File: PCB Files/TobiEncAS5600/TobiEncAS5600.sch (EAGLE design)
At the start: 4 parts

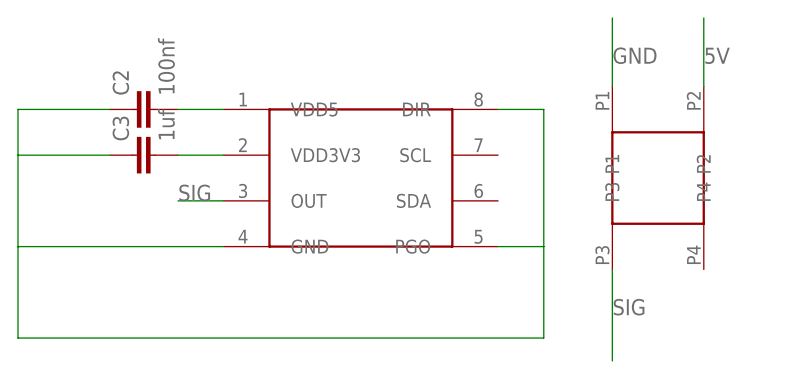
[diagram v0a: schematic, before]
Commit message: position components for wider encoder board
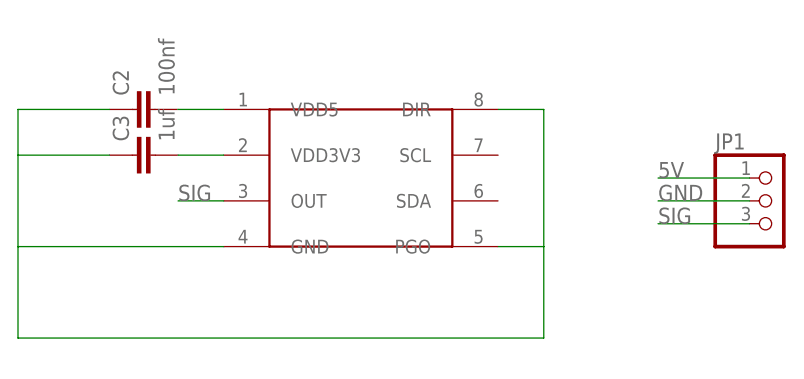
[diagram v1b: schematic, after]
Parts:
- removed U$2: DF11-4PIN, Gavin:DF11-4PIN
- added JP1: (no value), pinhead:PINHD-1X3
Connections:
- net N$1 renamed VDD3V3
- net 5V: now also JP1.1; no longer U$2.P2
- net GND: now also JP1.2; no longer U$2.P1
- net SIG: now also JP1.3; no longer U$2.P3
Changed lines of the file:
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@@
 <?xml version="1.0" encoding="utf-8"?>
 <!DOCTYPE eagle SYSTEM "eagle.dtd">
-<eagle version="6.4">
+<eagle version="8.5.2">
 <drawing>
 <settings>
-<setting alwaysvectorfont="yes"/>
+<setting alwaysvectorfont="no"/>
+<setting keepoldvectorfont="yes"/>
 <setting verticaltext="up"/>
 </settings>
@@
 </classes>
 <parts>
-<part name="U$2" library="Gavin" deviceset="DF11-4PIN" device=""/>
 <part name="U$1" library="Gavin" deviceset="AS5600" device=""/>
 <part name="C2" library="SparkFun-Capacitors" deviceset="CAP" device="0603-CAP" value="100nf"/>
 <part name="C3" library="SparkFun-Capacitors" deviceset="CAP" device="0603-CAP" value="1uf"/>
+<part name="JP1" library="pinhead" library_urn="urn:adsk.eagle:library:325" deviceset="PINHD-1X3" device=""/>
 </parts>
 <sheets>
@@
 </plain>
 <instances>
-<instance part="U$2" gate="G$1" x="106.68" y="60.96"/>
 <instance part="U$1" gate="G$1" x="73.66" y="60.96"/>
 <instance part="C2" gate="G$1" x="50.8" y="68.58" rot="R90"/>
 <instance part="C3" gate="G$1" x="50.8" y="63.5" rot="R90"/>
+<instance part="JP1" gate="A" x="119.38" y="58.42"/>
 </instances>
 <busses>
@@
 <net name="5V" class="0">
 <segment>
-<pinref part="U$2" gate="G$1" pin="P2"/>
-<wire x1="111.76" y1="71.12" x2="111.76" y2="78.74" width="0.1524" layer="91"/>
-<label x="111.76" y="73.66" size="1.778" layer="95"/>
-</segment>
-<segment>
 <pinref part="U$1" gate="G$1" pin="VDD5"/>
 <wire x1="58.42" y1="68.58" x2="53.34" y2="68.58" width="0.1524" layer="91"/>
 <pinref part="C2" gate="G$1" pin="2"/>
 </segment>
+<segment>
+<pinref part="JP1" gate="A" pin="1"/>
+<wire x1="116.84" y1="60.96" x2="106.68" y2="60.96" width="0.1524" layer="91"/>
+<label x="106.68" y="60.96" size="1.778" layer="95"/>
+</segment>
 </net>
 <net name="SIG" class="0">
-<segment>
-<pinref part="U$2" gate="G$1" pin="P3"/>
-<wire x1="101.6" y1="40.64" x2="101.6" y2="50.8" width="0.1524" layer="91"/>
-<label x="101.6" y="45.72" size="1.778" layer="95"/>
-</segment>
 <segment>
 <pinref part="U$1" gate="G$1" pin="OUT"/>
@@
 <label x="53.34" y="58.42" size="1.778" layer="95"/>
 </segment>
+<segment>
+<pinref part="JP1" gate="A" pin="3"/>
+<wire x1="116.84" y1="55.88" x2="106.68" y2="55.88" width="0.1524" layer="91"/>
+<label x="106.68" y="55.88" size="1.778" layer="95"/>
+</segment>
 </net>
 <net name="GND" class="0">
-<segment>
-<pinref part="U$2" gate="G$1" pin="P1"/>
-<wire x1="101.6" y1="78.74" x2="101.6" y2="71.12" width="0.1524" layer="91"/>
-<label x="101.6" y="73.66" size="1.778" layer="95"/>
-</segment>
 <segment>
 <pinref part="C2" gate="G$1" pin="1"/>
@@
 <wire x1="45.72" y1="63.5" x2="35.56" y2="63.5" width="0.1524" layer="91"/>
 </segment>
-</net>
-<net name="N$1" class="0">
+<segment>
+<pinref part="JP1" gate="A" pin="2"/>
+<wire x1="116.84" y1="58.42" x2="106.68" y2="58.42" width="0.1524" layer="91"/>
+<label x="106.68" y="58.42" size="1.778" layer="95"/>
+</segment>
+</net>
+<net name="VDD3V3" class="0">
 <segment>
 <pinref part="C3" gate="G$1" pin="2"/>
@@
 </schematic>
 </drawing>
+<compatibility>
+<note version="8.2" severity="warning">
+Since Version 8.2, EAGLE supports online libraries. The ids
+of those online libraries will not be understood (or retained)
+with this version.
+</note>
+</compatibility>
 </eagle>

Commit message: double wide encoder board
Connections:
- net GND: now also U$1.SCL, U$1.SDA
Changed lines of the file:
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@@
 <pinref part="U$1" gate="G$1" pin="DIR"/>
 <wire x1="88.9" y1="68.58" x2="93.98" y2="68.58" width="0.1524" layer="91"/>
-<wire x1="93.98" y1="68.58" x2="93.98" y2="53.34" width="0.1524" layer="91"/>
+<wire x1="93.98" y1="68.58" x2="93.98" y2="63.5" width="0.1524" layer="91"/>
+<wire x1="93.98" y1="63.5" x2="93.98" y2="58.42" width="0.1524" layer="91"/>
+<wire x1="93.98" y1="58.42" x2="93.98" y2="53.34" width="0.1524" layer="91"/>
 <wire x1="93.98" y1="53.34" x2="93.98" y2="43.18" width="0.1524" layer="91"/>
 <wire x1="93.98" y1="43.18" x2="35.56" y2="43.18" width="0.1524" layer="91"/>
@@
 <pinref part="U$1" gate="G$1" pin="PGO"/>
 <wire x1="88.9" y1="53.34" x2="93.98" y2="53.34" width="0.1524" layer="91"/>
+<pinref part="U$1" gate="G$1" pin="SCL"/>
+<wire x1="88.9" y1="63.5" x2="93.98" y2="63.5" width="0.1524" layer="91"/>
+<junction x="93.98" y="63.5"/>
+<pinref part="U$1" gate="G$1" pin="SDA"/>
+<wire x1="88.9" y1="58.42" x2="93.98" y2="58.42" width="0.1524" layer="91"/>
+<junction x="93.98" y="58.42"/>
 </segment>
 <segment>
